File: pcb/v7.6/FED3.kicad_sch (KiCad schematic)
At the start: 37 parts, among them IC2 TB6612FNG, J2 Conn_01x02_Odd_Even, J3 USB4105-GF-A, SW1 Sw, U2 MIC5504-3.3, U3 MCP73834-xxxx, X3 B2B-PH-K-S

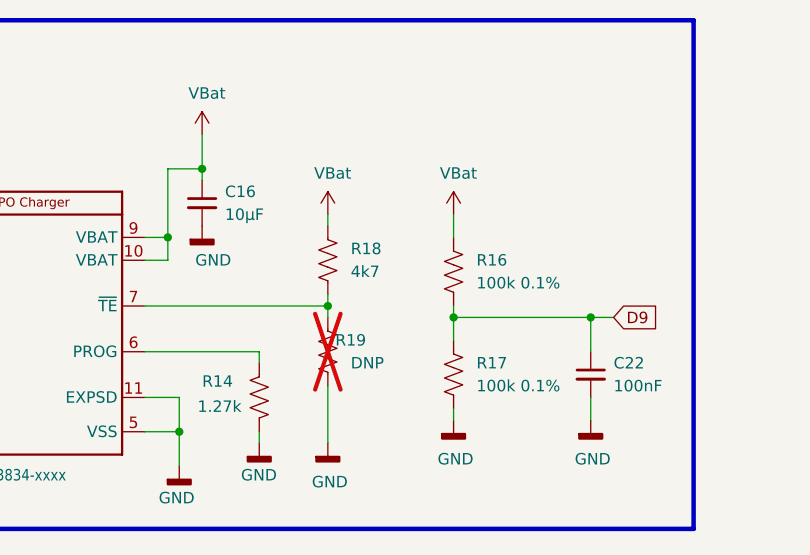
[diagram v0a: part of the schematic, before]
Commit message: PUp de Battery Charge
- modificado valor R18 - R para setup de I Batt charge
- actualizada PCB & BOM
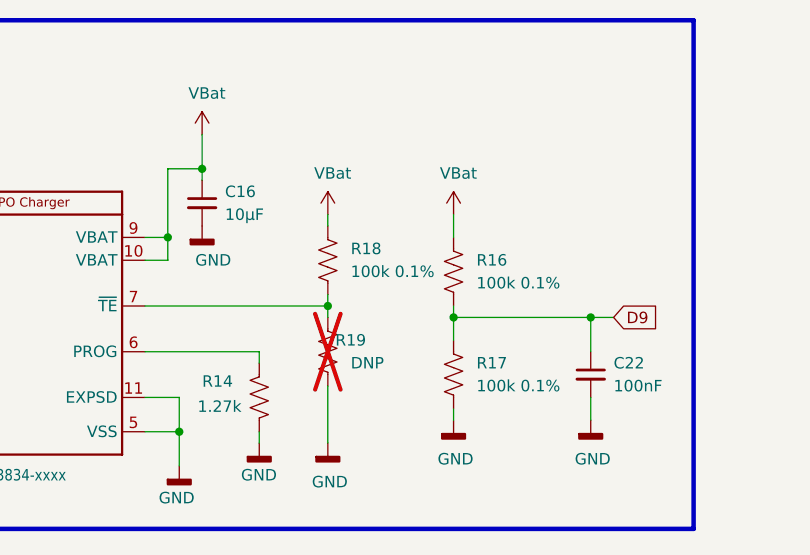
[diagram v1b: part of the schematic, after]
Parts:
- R18: value 4k7 -> 100k 0.1%; MPN ERJ-2RKF4701X -> RG1005P-104-B-T5; OEPSPN OEPS020010 -> OEPS020175
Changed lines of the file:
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@@
 			)
 		)
-		(property "Value" "4k7"
+		(property "Value" "100k 0.1%"
 			(at 241.3 41.9099 0)
 			(effects
@@
 			)
 		)
-		(property "OEPSPN" "OEPS020010"
+		(property "OEPSPN" "OEPS020175"
 			(at 238.76 40.64 0)
 			(effects
@@
 			)
 		)
-		(property "MPN" "ERJ-2RKF4701X"
+		(property "MPN" "RG1005P-104-B-T5"
 			(at 238.76 40.64 0)
 			(effects
